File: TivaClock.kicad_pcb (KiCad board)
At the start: 2 copper layers, 7 parts, among them J1 Conn_01x10, J2 Conn_01x10, J3 Conn_01x10, J4 Conn_01x10, J5 Conn_01x20, J6 Conn_01x20, J7 GS3

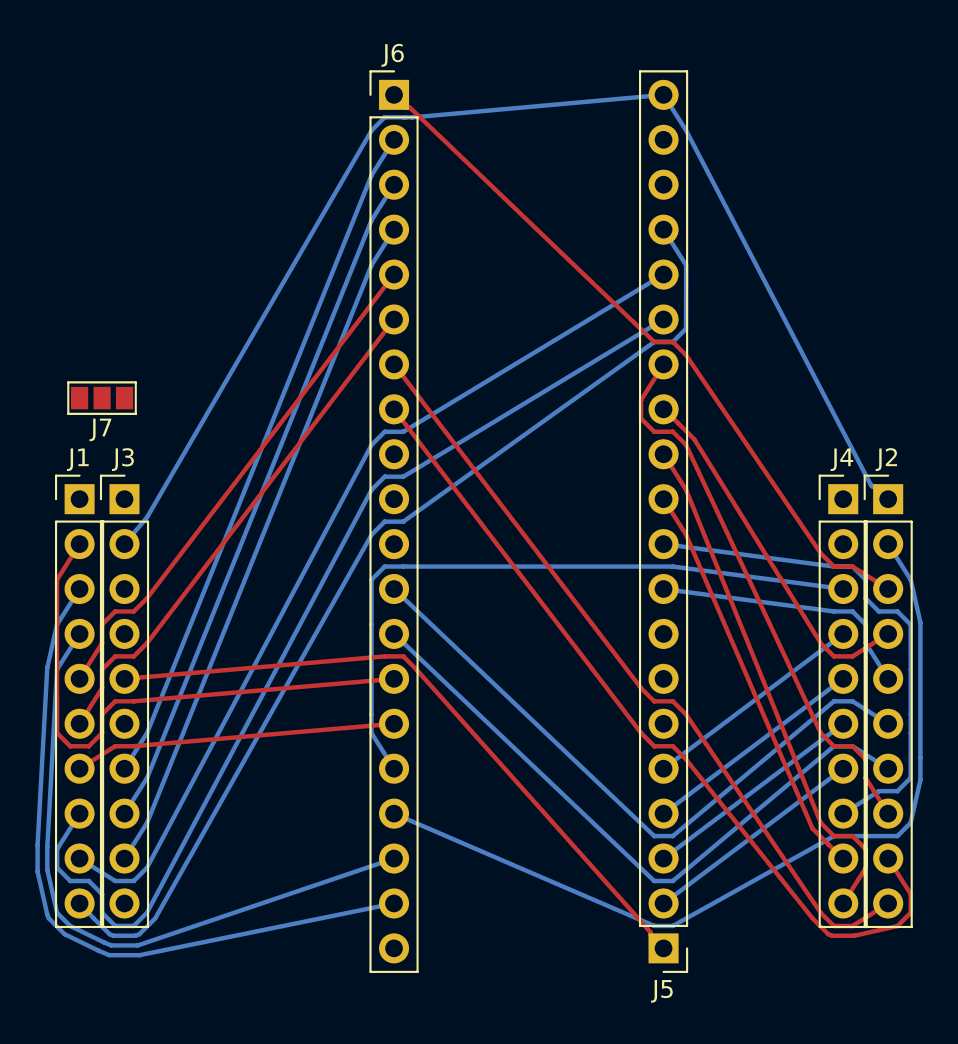
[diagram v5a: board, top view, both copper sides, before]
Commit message: reroute with solder jumper
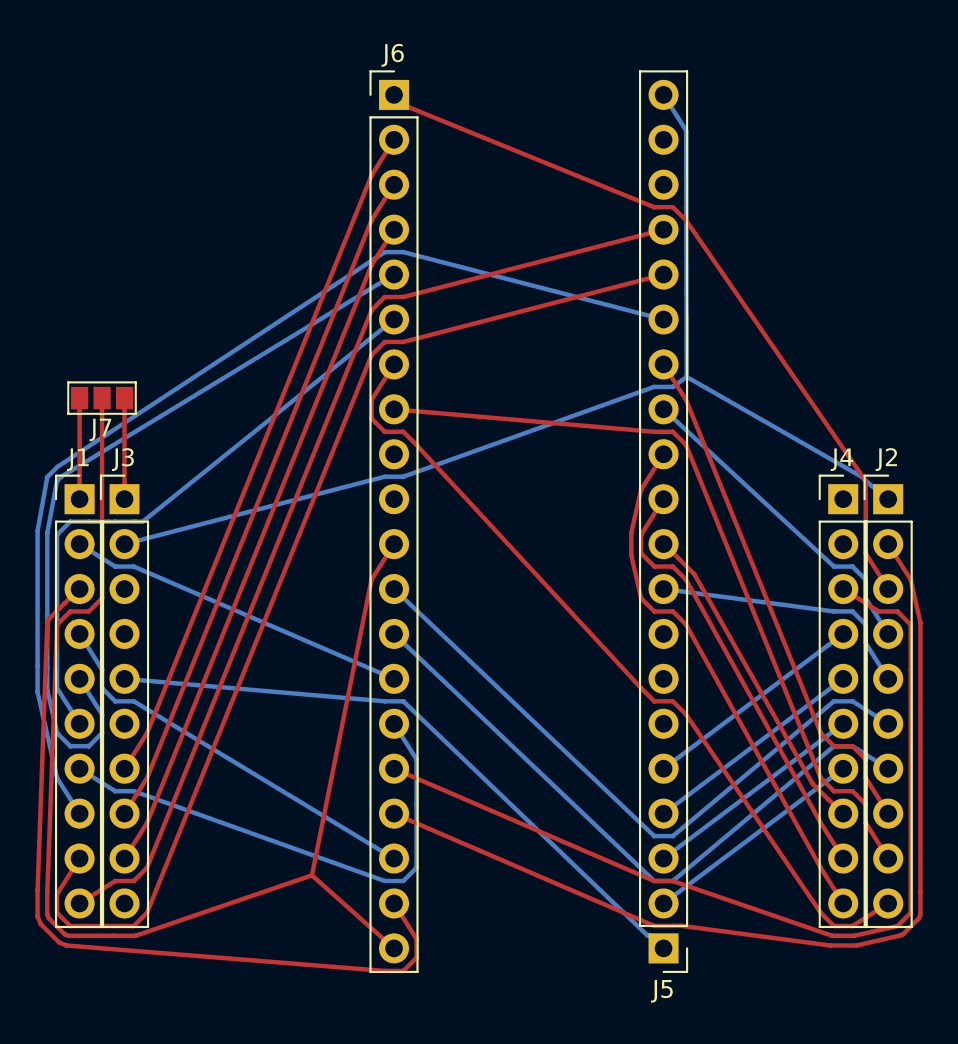
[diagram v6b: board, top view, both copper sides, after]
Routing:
- net /VCC: track 0.00 -> 72.6 mm
- net /X3: track 38.1 -> 52.2 mm
- net /X1: track 36.6 -> 22.7 mm
- net /Bit4: track 29.6 -> 43.3 mm
- net /X5: track 32.1 -> 19.5 mm
- net /X4: track 18.2 -> 29.1 mm
- net /RXD: track 29.2 -> 18.5 mm
- net /Bit10: track 50.9 -> 60.4 mm
- net /GND: track 70.4 -> 63.1 mm
- net Net-(J3-Pad1): track 0.00 -> 5.71 mm
- net Net-(J1-Pad1): track 0.00 -> 5.71 mm
- net /X0: track 39.6 -> 45.3 mm
- net /Bit5: track 29.6 -> 34.4 mm
- net /X2: track 48.4 -> 53.1 mm
- net /Bit7: track 47.4 -> 43.8 mm
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
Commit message: save n exit
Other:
- board outline added: 52.7 x 54 mm
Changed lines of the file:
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@@
   (general
     (links 36)
-    (no_connects 36)
+    (no_connects 0)
     (area 96.852381 75.435 152.06762 130.405)
     (thickness 1.6)
-    (drawings 0)
+    (drawings 4)
     (tracks 350)
     (zones 0)
@@
     (visible_elements 7FFFFFFF)
     (pcbplotparams
-      (layerselection 0x00030_80000001)
-      (usegerberextensions false)
+      (layerselection 0x010f0_80000001)
+      (usegerberextensions true)
       (excludeedgelayer true)
       (linewidth 0.100000)
@@
       (outputformat 1)
       (mirror false)
-      (drillshape 1)
+      (drillshape 0)
       (scaleselection 1)
-      (outputdirectory ""))
+      (outputdirectory Gerbers/))
   )
   (net 0 "")
@@
       (net 21 "Net-(J3-Pad1)"))
   )
+  (gr_line (start 97.79 75.565) (end 150.495 75.565) (angle 90) (layer Edge.Cuts) (width 0.15))
+  (gr_line (start 97.79 129.54) (end 97.79 75.565) (angle 90) (layer Edge.Cuts) (width 0.15))
+  (gr_line (start 150.495 129.54) (end 97.79 129.54) (angle 90) (layer Edge.Cuts) (width 0.15))
+  (gr_line (start 150.495 129.54) (end 150.495 75.565) (angle 90) (layer Edge.Cuts) (width 0.15))
   (segment (start 101.6 100.875) (end 101.6 101.6) (width 0.25) (layer F.Cu) (net 1))
   (segment (start 101.6 100.75) (end 101.6 100.875) (width 0.25) (layer F.Cu) (net 1))
